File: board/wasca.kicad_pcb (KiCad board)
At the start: 2 copper layers, 100.1 x 77.4 mm, 109 parts, among them CN1 CARTRIDGE_EDGE_CONNECTOR, CN2 TFP09-2-12B, CN3 Conn_02x02_Odd_Even, CN4 Conn_02x02_Odd_Even, CN5 Conn_02x03_Odd_Even, CN6 USB_C_Receptacle_USB2.0, CN7 Conn_02x05_Odd_Even, SW1 Conn_01x03_Male, U1 74ALVC164245, U10 SN74LVC1T45DBV, U11 SN74LVC1T45DBV, U12 SN74LVC1T45DBV, U13 ESP32_CAM_HALF, U2 74ALVC164245, U3 10M08SCE144C8G, U4 LD1117S33TR_SOT223, U5 74ALVC164245, U6 STM32F446RETx, U7 SDRAM_MT48_x16, U8 SN74LVC1T45DBV, U9 SN74LVC1T45DBV, Y1 Crystal

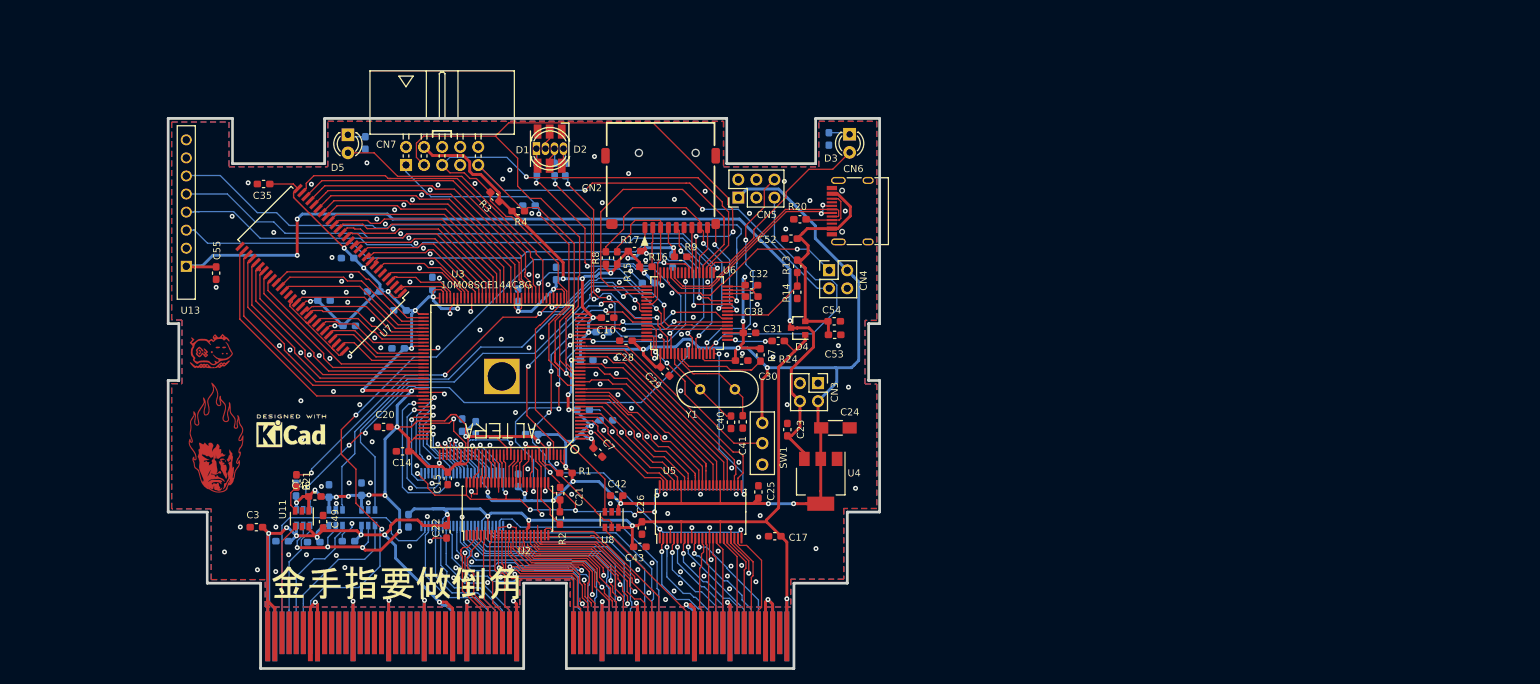
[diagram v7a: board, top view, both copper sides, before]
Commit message: SODIMM based board (preliminary work)
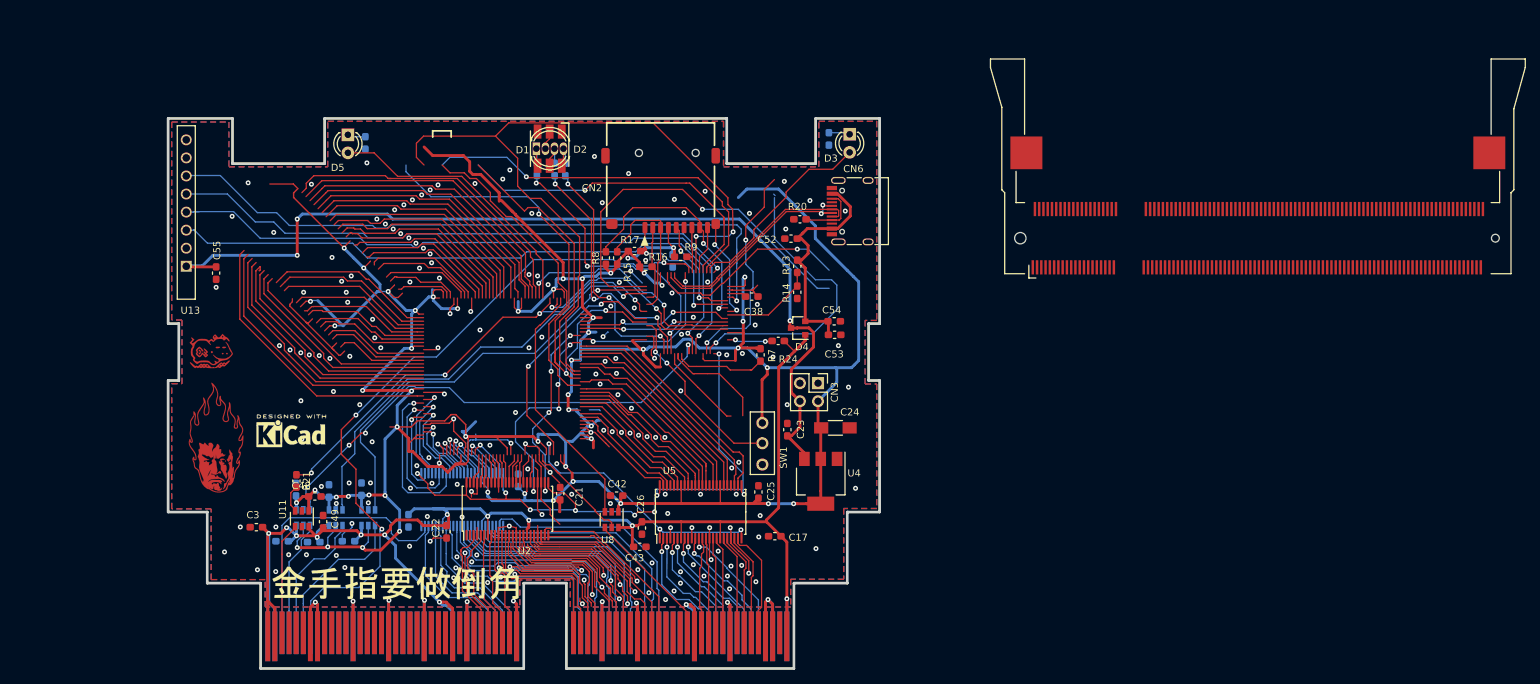
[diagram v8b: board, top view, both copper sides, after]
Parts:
- removed C10, C11, C12, C13, C14, C15, C16, C18, C19, C20, C27, C28, C29, C30, C31, C32, C33, C34, C35, C36, C37, C4, C5, C6, C7, C8, C9: 0.1uF, Capacitor_SMD:C_0603_1608Metric_Pad1.05x0.95mm_HandSolder
- removed C40, C41: 22pF, Capacitor_SMD:C_0603_1608Metric_Pad1.05x0.95mm_HandSolder
- removed CN5: Conn_02x03_Odd_Even, Connector_PinHeader_2.54mm:PinHeader_2x03_P2.54mm_Vertical
- removed CN7: Conn_02x05_Odd_Even, wasca:Multicomp_MC9A22-1034_2x05_P2.54mm_Horizontal
- removed R1, R2, R3, R4, R5: 10K, Capacitor_SMD:C_0603_1608Metric_Pad1.05x0.95mm_HandSolder
- removed R6: 1K, Capacitor_SMD:C_0603_1608Metric_Pad1.05x0.95mm_HandSolder
- removed U3: 10M08SCE144C8G, wasca:TQFP144_ALTERA_HANDSOLDERING
- removed U6: STM32F446RETx, Package_QFP:LQFP-64_10x10mm_P0.5mm
- removed U7: SDRAM_MT48_x16, wasca:TSOP-II-54_22.2x10.16mm_P0.8mm
- removed Y1: Crystal, Crystal:Crystal_HC49-4H_Vertical
- CN4: value Conn_02x02_Odd_Even -> SODIMM-200; footprint Connector_PinHeader_2.54mm:PinHeader_2x02_P2.54mm_Vertical -> wasca:Conn_TE-DDR2-SODIMM-0.6-200P-doublesided
- moved CN4 60.5 mm to (180.1, 97.8), turned to 90 degrees
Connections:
- CN4 pad 1: /SWDIO -> Net-(CN4-Pad1)
- CN4 pad 2: /+3_3V -> Net-(CN4-Pad2)
- CN4 pad 3: /SWCLK -> Net-(CN4-Pad3)
- CN4 pad 4: GND -> Net-(CN4-Pad4)
- R7 pad 1: Net-(R7-Pad1) -> Net-(CN4-Pad137)
- SW1 pad 2: Net-(SW1-Pad2) -> Net-(CN4-Pad141)
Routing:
- net Net-(SW1-Pad2): track 25.3 -> 0.00 mm, vias 2 -> 0
- net Net-(CN4-Pad141): track 0.00 -> 25.3 mm, vias 0 -> 2
- net Net-(R7-Pad1): track 13.0 -> 0.00 mm
- net Net-(CN4-Pad137): track 0.00 -> 13.0 mm
